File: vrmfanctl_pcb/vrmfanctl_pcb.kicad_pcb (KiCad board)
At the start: 2 copper layers, 27.9 x 33.3 mm, 14 parts, among them J1 SATA Power Male, J2 Pin header L-shape, J3 Pin socket L-shape, J4 Pin socket L-shape, Q1 2SC1740, Q2 2SC1740, Q3 2SC1740, U1 ATtiny85-20PU

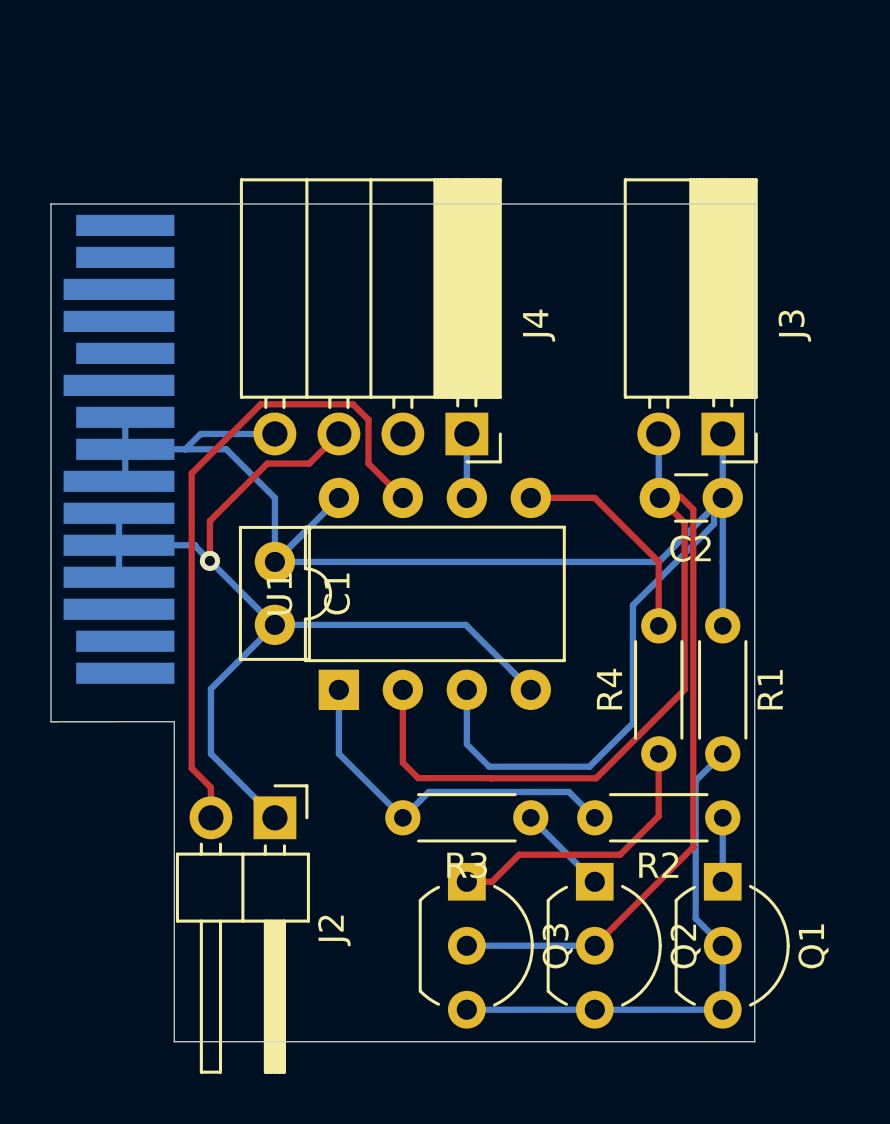
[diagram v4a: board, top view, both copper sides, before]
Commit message: swap PB2 and PB0
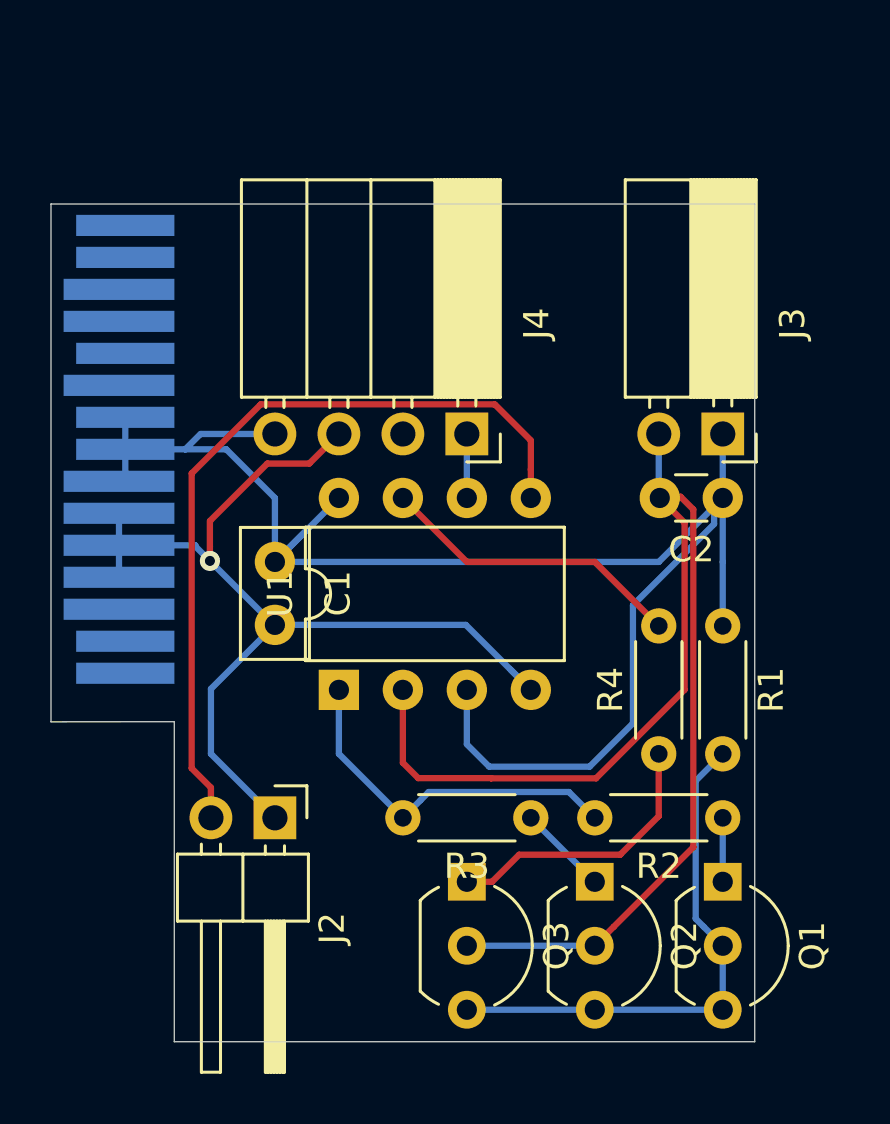
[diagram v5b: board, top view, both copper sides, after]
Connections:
- J1 pad 1: (no net) -> Net-(J1-Pad1)
- J1 pad 10: (no net) -> Net-(J1-Pad10)
- J1 pad 11: (no net) -> Net-(J1-Pad11)
- J1 pad 12: (no net) -> Net-(J1-Pad12)
- J1 pad 13: (no net) -> Net-(J1-Pad13)
- J1 pad 14: (no net) -> Net-(J1-Pad14)
- J1 pad 15: (no net) -> Net-(J1-Pad15)
- J1 pad 2: (no net) -> Net-(J1-Pad2)
- J1 pad 3: (no net) -> Net-(J1-Pad3)
- J4 pad 2: (no net) -> Net-(J4-Pad2)
- U1 pad 5: /BDPWR200 -> /TX_RX
- U1 pad 7: /TX_RX -> /BDPWR200
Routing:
- net /TX_RX: track 26.1 -> 31.5 mm
- net /BDPWR200: track 8.67 -> 12.3 mm
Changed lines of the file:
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@@
-(kicad_pcb (version 20171130) (host pcbnew 5.1.4-e60b266~84~ubuntu18.04.1)
+(kicad_pcb (version 20171130) (host pcbnew 5.0.2+dfsg1-1)
   (general
     (thickness 1.6)
     (drawings 6)
-    (tracks 96)
+    (tracks 95)
     (zones 0)
     (modules 14)
-    (nets 12)
+    (nets 22)
   )
   (page A4)
@@
     (zone_45_only no)
     (trace_min 0.2)
+    (segment_width 0.2)
+    (edge_width 0.05)
     (via_size 0.8)
     (via_drill 0.4)
@@
     (uvia_min_size 0.2)
     (uvia_min_drill 0.1)
-    (edge_width 0.05)
-    (segment_width 0.2)
     (pcb_text_width 0.3)
     (pcb_text_size 1.5 1.5)
@@
   (net 10 /BDPWR200)
   (net 11 /TX_RX)
+  (net 12 "Net-(J1-Pad15)")
+  (net 13 "Net-(J1-Pad14)")
+  (net 14 "Net-(J1-Pad13)")
+  (net 15 "Net-(J1-Pad12)")
+  (net 16 "Net-(J1-Pad11)")
+  (net 17 "Net-(J1-Pad10)")
+  (net 18 "Net-(J1-Pad3)")
+  (net 19 "Net-(J1-Pad2)")
+  (net 20 "Net-(J1-Pad1)")
+  (net 21 "Net-(J4-Pad2)")
   (net_class Default "これはデフォルトのネット クラスです。"
     (clearance 0.2)
@@
     (pad 1 thru_hole rect (at 0 0 270) (size 1.7 1.7) (drill 1) (layers *.Cu *.Mask)
       (net 3 /PWM))
-    (pad 2 thru_hole oval (at 0 2.54 270) (size 1.7 1.7) (drill 1) (layers *.Cu *.Mask))
+    (pad 2 thru_hole oval (at 0 2.54 270) (size 1.7 1.7) (drill 1) (layers *.Cu *.Mask)
+      (net 21 "Net-(J4-Pad2)"))
     (pad 3 thru_hole oval (at 0 5.08 270) (size 1.7 1.7) (drill 1) (layers *.Cu *.Mask)
       (net 2 GND))
@@
       (net 2 GND))
     (pad 7 thru_hole oval (at 7.62 2.54 90) (size 1.6 1.6) (drill 0.8) (layers *.Cu *.Mask)
-      (net 11 /TX_RX))
+      (net 10 /BDPWR200))
     (pad 3 thru_hole oval (at 0 5.08 90) (size 1.6 1.6) (drill 0.8) (layers *.Cu *.Mask)
       (net 1 VCC))
@@
       (net 4 /D-))
     (pad 5 thru_hole oval (at 7.62 7.62 90) (size 1.6 1.6) (drill 0.8) (layers *.Cu *.Mask)
-      (net 10 /BDPWR200))
+      (net 11 /TX_RX))
     (pad 1 thru_hole rect (at 0 0 90) (size 1.6 1.6) (drill 0.8) (layers *.Cu *.Mask)
       (net 9 /BDPWR10))
@@
     (fp_line (start -19.05 0) (end -19.05 4.9) (layer B.SilkS) (width 0.12))
     (fp_line (start 1.52 0) (end -19.05 0) (layer B.SilkS) (width 0.12))
-    (pad 15 smd rect (at -18.2 1.95 270) (size 0.84 3.9) (layers B.Cu B.Paste B.Mask))
-    (pad 14 smd rect (at -16.93 1.95 270) (size 0.84 3.9) (layers B.Cu B.Paste B.Mask))
-    (pad 13 smd rect (at -15.66 2.2 270) (size 0.84 4.4) (layers B.Cu B.Paste B.Mask))
-    (pad 12 smd rect (at -14.39 2.2 270) (size 0.84 4.4) (layers B.Cu B.Paste B.Mask))
-    (pad 11 smd rect (at -13.12 1.95 270) (size 0.84 3.9) (layers B.Cu B.Paste B.Mask))
-    (pad 10 smd rect (at -11.85 2.2 270) (size 0.84 4.4) (layers B.Cu B.Paste B.Mask))
+    (pad 15 smd rect (at -18.2 1.95 270) (size 0.84 3.9) (layers B.Cu B.Paste B.Mask)
+      (net 12 "Net-(J1-Pad15)"))
+    (pad 14 smd rect (at -16.93 1.95 270) (size 0.84 3.9) (layers B.Cu B.Paste B.Mask)
+      (net 13 "Net-(J1-Pad14)"))
+    (pad 13 smd rect (at -15.66 2.2 270) (size 0.84 4.4) (layers B.Cu B.Paste B.Mask)
+      (net 14 "Net-(J1-Pad13)"))
+    (pad 12 smd rect (at -14.39 2.2 270) (size 0.84 4.4) (layers B.Cu B.Paste B.Mask)
+      (net 15 "Net-(J1-Pad12)"))
+    (pad 11 smd rect (at -13.12 1.95 270) (size 0.84 3.9) (layers B.Cu B.Paste B.Mask)
+      (net 16 "Net-(J1-Pad11)"))
+    (pad 10 smd rect (at -11.85 2.2 270) (size 0.84 4.4) (layers B.Cu B.Paste B.Mask)
+      (net 17 "Net-(J1-Pad10)"))
     (pad 9 smd rect (at -10.58 1.95 270) (size 0.84 3.9) (layers B.Cu B.Paste B.Mask)
       (net 1 VCC))
@@
     (pad 4 smd rect (at -4.23 2.2 270) (size 0.84 4.4) (layers B.Cu B.Paste B.Mask)
       (net 2 GND))
-    (pad 3 smd rect (at -2.96 2.2 270) (size 0.84 4.4) (layers B.Cu B.Paste B.Mask))
-    (pad 2 smd rect (at -1.69 1.95 270) (size 0.84 3.9) (layers B.Cu B.Paste B.Mask))
-    (pad 1 smd rect (at -0.42 1.95 270) (size 0.84 3.9) (layers B.Cu B.Paste B.Mask))
+    (pad 3 smd rect (at -2.96 2.2 270) (size 0.84 4.4) (layers B.Cu B.Paste B.Mask)
+      (net 18 "Net-(J1-Pad3)"))
+    (pad 2 smd rect (at -1.69 1.95 270) (size 0.84 3.9) (layers B.Cu B.Paste B.Mask)
+      (net 19 "Net-(J1-Pad2)"))
+    (pad 1 smd rect (at -0.42 1.95 270) (size 0.84 3.9) (layers B.Cu B.Paste B.Mask)
+      (net 20 "Net-(J1-Pad1)"))
   )
   (module Connector_PinSocket_2.54mm:PinSocket_1x02_P2.54mm_Horizontal (layer F.Cu)
@@
   (segment (start 57.394999 65.014999) (end 51.825001 65.014999) (width 0.25) (layer B.Cu) (net 9))
   (segment (start 58.42 66.04) (end 57.394999 65.014999) (width 0.25) (layer B.Cu) (net 9))
-  (segment (start 55.88 53.34) (end 58.42 53.34) (width 0.25) (layer F.Cu) (net 10))
-  (segment (start 58.42 53.34) (end 60.96 55.88) (width 0.25) (layer F.Cu) (net 10))
-  (segment (start 60.96 55.88) (end 60.96 58.42) (width 0.25) (layer F.Cu) (net 10))
-  (segment (start 45.155999 49.624999) (end 42.414999 52.365999) (width 0.25) (layer F.Cu) (net 11))
-  (segment (start 43.18 64.837919) (end 43.18 66.04) (width 0.25) (layer F.Cu) (net 11))
-  (segment (start 42.414999 64.072918) (end 43.18 64.837919) (width 0.25) (layer F.Cu) (net 11))
-  (segment (start 42.414999 52.365999) (end 42.414999 64.072918) (width 0.25) (layer F.Cu) (net 11))
-  (segment (start 50.000001 52.540001) (end 50.8 53.34) (width 0.25) (layer F.Cu) (net 11))
-  (segment (start 49.435001 51.975001) (end 50.000001 52.540001) (width 0.25) (layer F.Cu) (net 11))
-  (segment (start 49.435001 50.235999) (end 49.435001 51.975001) (width 0.25) (layer F.Cu) (net 11))
-  (segment (start 48.824001 49.624999) (end 49.435001 50.235999) (width 0.25) (layer F.Cu) (net 11))
-  (segment (start 45.155999 49.624999) (end 48.824001 49.624999) (width 0.25) (layer F.Cu) (net 11))
+  (segment (start 50.8 53.34) (end 53.34 55.88) (width 0.25) (layer F.Cu) (net 10))
+  (segment (start 58.42 55.88) (end 60.96 58.42) (width 0.25) (layer F.Cu) (net 10))
+  (segment (start 53.34 55.88) (end 58.42 55.88) (width 0.25) (layer F.Cu) (net 10))
+  (segment (start 54.450001 49.624999) (end 55.88 51.054998) (width 0.25) (layer F.Cu) (net 11))
+  (segment (start 43.18 66.04) (end 43.18 64.837919) (width 0.25) (layer F.Cu) (net 11))
+  (segment (start 55.88 51.054998) (end 55.88 52.20863) (width 0.25) (layer F.Cu) (net 11))
+  (segment (start 42.414999 52.365999) (end 45.155999 49.624999) (width 0.25) (layer F.Cu) (net 11))
+  (segment (start 43.18 64.837919) (end 42.414999 64.072918) (width 0.25) (layer F.Cu) (net 11))
+  (segment (start 42.414999 64.072918) (end 42.414999 52.365999) (width 0.25) (layer F.Cu) (net 11))
+  (segment (start 55.88 52.20863) (end 55.88 53.34) (width 0.25) (layer F.Cu) (net 11))
+  (segment (start 45.155999 49.624999) (end 54.450001 49.624999) (width 0.25) (layer F.Cu) (net 11))
 )

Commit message: update pcb layout
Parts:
- removed C2: 470p, Capacitor_THT:C_Disc_D3.0mm_W1.6mm_P2.50mm
- removed J4: Pin socket L-shape, Connector_PinSocket_2.54mm:PinSocket_1x04_P2.54mm_Horizontal
- removed Q1, Q2, Q3: 2SC1740, Package_TO_SOT_THT:TO-92_Inline_Wide
- removed R2, R3: 390k, Resistor_THT:R_Axial_DIN0204_L3.6mm_D1.6mm_P5.08mm_Horizontal
- removed R4: 20k, Resistor_THT:R_Axial_DIN0204_L3.6mm_D1.6mm_P5.08mm_Horizontal
- J2: value Pin header L-shape -> Pin socket L-shape; footprint Connector_PinHeader_2.54mm:PinHeader_1x02_P2.54mm_Horizontal -> Connector_PinSocket_2.54mm:PinSocket_1x04_P2.54mm_Horizontal
- R1: value 56k -> 3.9k
- moved J2 17.0 mm to (53.3, 50.8)
- moved R1 3.59 mm to (61.0, 61.0), turned to 90 degrees
- moved J3 2.54 mm to (61.0, 50.8)
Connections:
- J1 pad 1: Net-(J1-Pad1) -> (no net)
- J1 pad 10: Net-(J1-Pad10) -> (no net)
- J1 pad 11: Net-(J1-Pad11) -> (no net)
- J1 pad 12: Net-(J1-Pad12) -> (no net)
- J1 pad 13: Net-(J1-Pad13) -> (no net)
- J1 pad 14: Net-(J1-Pad14) -> (no net)
- J1 pad 15: Net-(J1-Pad15) -> (no net)
- J1 pad 2: Net-(J1-Pad2) -> (no net)
- J1 pad 3: Net-(J1-Pad3) -> (no net)
- J2 pad 1: GND -> /PWM
- J2 pad 2: /TX_RX -> (no net)
- J3 pad 1: VCC -> Net-(J3-Pad1)
- J3 pad 2: /D- -> GND
- R1 pad 1: VCC -> /THMPWR
- R1 pad 2: Net-(Q1-Pad2) -> Net-(J3-Pad1)
- U1 pad 1: /BDPWR10 -> (no net)
- U1 pad 2: /D- -> /THMPWR
- U1 pad 3: VCC -> Net-(J3-Pad1)
- U1 pad 5: /TX_RX -> (no net)
- U1 pad 7: /BDPWR200 -> (no net)
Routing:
- net /D-: track 52.1 -> 0.00 mm
- net VCC: track 69.6 -> 20.3 mm
- net /TX_RX: track 31.5 -> 0.00 mm
- net Net-(Q1-Pad2): track 21.2 -> 0.00 mm
- net Net-(J3-Pad1): track 0.00 -> 18.1 mm
- net /BDPWR10: track 14.6 -> 0.00 mm
- net /THMPWR: track 0.00 -> 12.3 mm
- net /BDPWR200: track 12.3 -> 0.00 mm
- net Net-(Q3-Pad1): track 11.2 -> 0.00 mm
- net Net-(Q2-Pad1): track 3.59 -> 0.00 mm
- net Net-(Q1-Pad1): track 2.54 -> 0.00 mm
- net GND: track 42.1 -> 39.6 mm
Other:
- board size 27.9 x 33.3 mm -> 25.4 x 23.1 mm

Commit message: update thermistor config. change R1 resistor to 4.7K.
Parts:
- R1: value 3.9k -> 4.7k
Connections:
- J1 pad 1: (no net) -> Net-(J1-Pad1)
- J1 pad 10: (no net) -> Net-(J1-Pad10)
- J1 pad 11: (no net) -> Net-(J1-Pad11)
- J1 pad 12: (no net) -> Net-(J1-Pad12)
- J1 pad 13: (no net) -> Net-(J1-Pad13)
- J1 pad 14: (no net) -> Net-(J1-Pad14)
- J1 pad 15: (no net) -> Net-(J1-Pad15)
- J1 pad 2: (no net) -> Net-(J1-Pad2)
- J1 pad 3: (no net) -> Net-(J1-Pad3)
- J2 pad 2: (no net) -> Net-(J2-Pad2)
- U1 pad 1: (no net) -> Net-(U1-Pad1)
- U1 pad 5: (no net) -> /TX_RX
- U1 pad 7: (no net) -> Net-(U1-Pad7)
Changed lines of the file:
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@@
-(kicad_pcb (version 20171130) (host pcbnew 5.1.4-e60b266~84~ubuntu18.04.1)
+(kicad_pcb (version 20171130) (host pcbnew 5.0.2+dfsg1-1)
   (general
     (thickness 1.6)
@@
     (zones 0)
     (modules 6)
-    (nets 6)
+    (nets 19)
   )
   (page A4)
@@
     (zone_45_only no)
     (trace_min 0.2)
+    (segment_width 0.2)
+    (edge_width 0.05)
     (via_size 0.8)
     (via_drill 0.4)
@@
     (uvia_min_size 0.2)
     (uvia_min_drill 0.1)
-    (edge_width 0.05)
-    (segment_width 0.2)
     (pcb_text_width 0.3)
     (pcb_text_size 1.5 1.5)
@@
   (net 4 "Net-(J3-Pad1)")
   (net 5 /THMPWR)
+  (net 6 "Net-(J1-Pad15)")
+  (net 7 "Net-(J1-Pad14)")
+  (net 8 "Net-(J1-Pad13)")
+  (net 9 "Net-(J1-Pad12)")
+  (net 10 "Net-(J1-Pad11)")
+  (net 11 "Net-(J1-Pad10)")
+  (net 12 "Net-(J1-Pad3)")
+  (net 13 "Net-(J1-Pad2)")
+  (net 14 "Net-(J1-Pad1)")
+  (net 15 "Net-(J2-Pad2)")
+  (net 16 "Net-(U1-Pad7)")
+  (net 17 /TX_RX)
+  (net 18 "Net-(U1-Pad1)")
   (net_class Default "これはデフォルトのネット クラスです。"
     (clearance 0.2)
@@
     (add_net /PWM)
     (add_net /THMPWR)
+    (add_net /TX_RX)
     (add_net GND)
     (add_net "Net-(J1-Pad1)")
@@
     (add_net "Net-(J2-Pad2)")
     (add_net "Net-(J3-Pad1)")
+    (add_net "Net-(U1-Pad1)")
+    (add_net "Net-(U1-Pad7)")
     (add_net VCC)
   )
@@
     (pad 3 thru_hole oval (at 0 5.08 270) (size 1.7 1.7) (drill 1) (layers *.Cu *.Mask)
       (net 2 GND))
-    (pad 2 thru_hole oval (at 0 2.54 270) (size 1.7 1.7) (drill 1) (layers *.Cu *.Mask))
+    (pad 2 thru_hole oval (at 0 2.54 270) (size 1.7 1.7) (drill 1) (layers *.Cu *.Mask)
+      (net 15 "Net-(J2-Pad2)"))
     (pad 1 thru_hole rect (at 0 0 270) (size 1.7 1.7) (drill 1) (layers *.Cu *.Mask)
       (net 3 /PWM))
@@
     (pad 4 thru_hole oval (at 0 7.62 90) (size 1.6 1.6) (drill 0.8) (layers *.Cu *.Mask)
       (net 2 GND))
-    (pad 7 thru_hole oval (at 7.62 2.54 90) (size 1.6 1.6) (drill 0.8) (layers *.Cu *.Mask))
+    (pad 7 thru_hole oval (at 7.62 2.54 90) (size 1.6 1.6) (drill 0.8) (layers *.Cu *.Mask)
+      (net 16 "Net-(U1-Pad7)"))
     (pad 3 thru_hole oval (at 0 5.08 90) (size 1.6 1.6) (drill 0.8) (layers *.Cu *.Mask)
       (net 4 "Net-(J3-Pad1)"))
@@
     (pad 2 thru_hole oval (at 0 2.54 90) (size 1.6 1.6) (drill 0.8) (layers *.Cu *.Mask)
       (net 5 /THMPWR))
-    (pad 5 thru_hole oval (at 7.62 7.62 90) (size 1.6 1.6) (drill 0.8) (layers *.Cu *.Mask))
-    (pad 1 thru_hole rect (at 0 0 90) (size 1.6 1.6) (drill 0.8) (layers *.Cu *.Mask))
+    (pad 5 thru_hole oval (at 7.62 7.62 90) (size 1.6 1.6) (drill 0.8) (layers *.Cu *.Mask)
+      (net 17 /TX_RX))
+    (pad 1 thru_hole rect (at 0 0 90) (size 1.6 1.6) (drill 0.8) (layers *.Cu *.Mask)
+      (net 18 "Net-(U1-Pad1)"))
     (model ${KISYS3DMOD}/Package_DIP.3dshapes/DIP-8_W7.62mm.wrl
       (at (xyz 0 0 0))
@@
       (effects (font (size 1 1) (thickness 0.15)))
     )
-    (fp_text value 3.9k (at 2.54 1.92 90) (layer F.Fab)
+    (fp_text value 4.7k (at 2.54 1.92 90) (layer F.Fab)
       (effects (font (size 1 1) (thickness 0.15)))
     )
@@
     (fp_line (start -19.05 0) (end -19.05 4.9) (layer B.SilkS) (width 0.12))
     (fp_line (start 1.52 0) (end -19.05 0) (layer B.SilkS) (width 0.12))
-    (pad 15 smd rect (at -18.2 1.95 270) (size 0.84 3.9) (layers B.Cu B.Paste B.Mask))
-    (pad 14 smd rect (at -16.93 1.95 270) (size 0.84 3.9) (layers B.Cu B.Paste B.Mask))
-    (pad 13 smd rect (at -15.66 2.2 270) (size 0.84 4.4) (layers B.Cu B.Paste B.Mask))
-    (pad 12 smd rect (at -14.39 2.2 270) (size 0.84 4.4) (layers B.Cu B.Paste B.Mask))
-    (pad 11 smd rect (at -13.12 1.95 270) (size 0.84 3.9) (layers B.Cu B.Paste B.Mask))
-    (pad 10 smd rect (at -11.85 2.2 270) (size 0.84 4.4) (layers B.Cu B.Paste B.Mask))
+    (pad 15 smd rect (at -18.2 1.95 270) (size 0.84 3.9) (layers B.Cu B.Paste B.Mask)
+      (net 6 "Net-(J1-Pad15)"))
+    (pad 14 smd rect (at -16.93 1.95 270) (size 0.84 3.9) (layers B.Cu B.Paste B.Mask)
+      (net 7 "Net-(J1-Pad14)"))
+    (pad 13 smd rect (at -15.66 2.2 270) (size 0.84 4.4) (layers B.Cu B.Paste B.Mask)
+      (net 8 "Net-(J1-Pad13)"))
+    (pad 12 smd rect (at -14.39 2.2 270) (size 0.84 4.4) (layers B.Cu B.Paste B.Mask)
+      (net 9 "Net-(J1-Pad12)"))
+    (pad 11 smd rect (at -13.12 1.95 270) (size 0.84 3.9) (layers B.Cu B.Paste B.Mask)
+      (net 10 "Net-(J1-Pad11)"))
+    (pad 10 smd rect (at -11.85 2.2 270) (size 0.84 4.4) (layers B.Cu B.Paste B.Mask)
+      (net 11 "Net-(J1-Pad10)"))
     (pad 9 smd rect (at -10.58 1.95 270) (size 0.84 3.9) (layers B.Cu B.Paste B.Mask)
       (net 1 VCC))
@@
     (pad 4 smd rect (at -4.23 2.2 270) (size 0.84 4.4) (layers B.Cu B.Paste B.Mask)
       (net 2 GND))
-    (pad 3 smd rect (at -2.96 2.2 270) (size 0.84 4.4) (layers B.Cu B.Paste B.Mask))
-    (pad 2 smd rect (at -1.69 1.95 270) (size 0.84 3.9) (layers B.Cu B.Paste B.Mask))
-    (pad 1 smd rect (at -0.42 1.95 270) (size 0.84 3.9) (layers B.Cu B.Paste B.Mask))
+    (pad 3 smd rect (at -2.96 2.2 270) (size 0.84 4.4) (layers B.Cu B.Paste B.Mask)
+      (net 12 "Net-(J1-Pad3)"))
+    (pad 2 smd rect (at -1.69 1.95 270) (size 0.84 3.9) (layers B.Cu B.Paste B.Mask)
+      (net 13 "Net-(J1-Pad2)"))
+    (pad 1 smd rect (at -0.42 1.95 270) (size 0.84 3.9) (layers B.Cu B.Paste B.Mask)
+      (net 14 "Net-(J1-Pad1)"))
   )
   (module Connector_PinSocket_2.54mm:PinSocket_1x02_P2.54mm_Horizontal (layer F.Cu)
